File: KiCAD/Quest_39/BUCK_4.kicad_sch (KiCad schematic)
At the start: 32 parts, among them U16 AD626ANZ, U17 INA226, U18 LTM4611EV-PBF, U19 MCP4151-502E/SN

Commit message: Fixed INA226 schem. mistake and further layout work
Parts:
- added C63: 100nF, Capacitor_SMD:C_0603_1608Metric, symbol Device:C
- renumbered C56 to C59, C57 to C60, C58 to C61, C59 to C62, C60 to C64, C61 to C65, C62 to C66, C63 to C67, C64 to C68, C65 to C69, C66 to C70, C67 to C71, C68 to C72, C69 to C73
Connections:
- net +5V: now also C63.1
- net GND: now also C63.2
- net PV_POS: no longer C59.1, C60.1, C61.1, C62.1, R38.2, R40.1, R43.1, U18.A1 (VIN), U18.A2 (VIN), U18.A3 (VIN), U18.A4 (VIN), U18.A5 (VIN), U18.A6 (VIN), U18.B1 (VIN), U18.B2 (VIN), U18.B3 (VIN), U18.B4 (VIN), U18.B5 (VIN), U18.B6 (VIN), U18.C1 (VIN), U18.C2 (VIN), U18.C3 (VIN), U18.C4 (VIN), U18.C5 (VIN), U18.C6 (VIN)
- net Vin-: no longer TP28.1, U16.5 (OUT), U17.8 (Vbus)
- new net: TP28.1, U16.5 (OUT), U17.8 (Vbus)
- new net BUCK_VIN: C59.1, C60.1, C61.1, C62.1, R38.2, R40.1, R43.1, U18.A1 (VIN), U18.A2 (VIN), U18.A3 (VIN), U18.A4 (VIN), U18.A5 (VIN), U18.A6 (VIN), U18.B1 (VIN), U18.B2 (VIN), U18.B3 (VIN), U18.B4 (VIN), U18.B5 (VIN), U18.B6 (VIN), U18.C1 (VIN), U18.C2 (VIN), U18.C3 (VIN), U18.C4 (VIN), U18.C5 (VIN), U18.C6 (VIN)

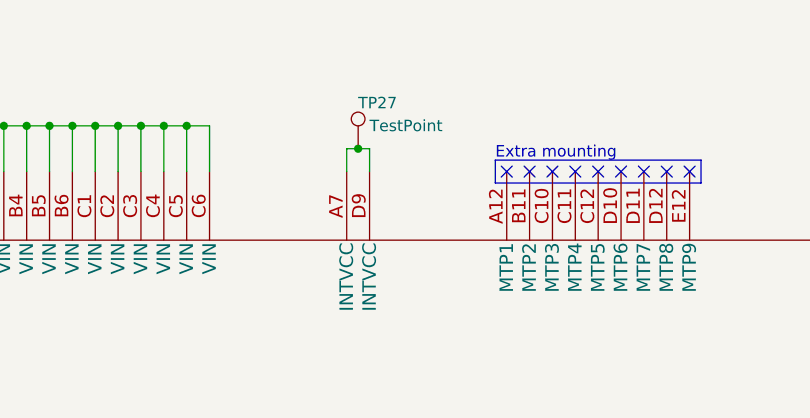
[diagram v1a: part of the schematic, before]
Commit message: Partial wiring of first buck converter section PCB layout
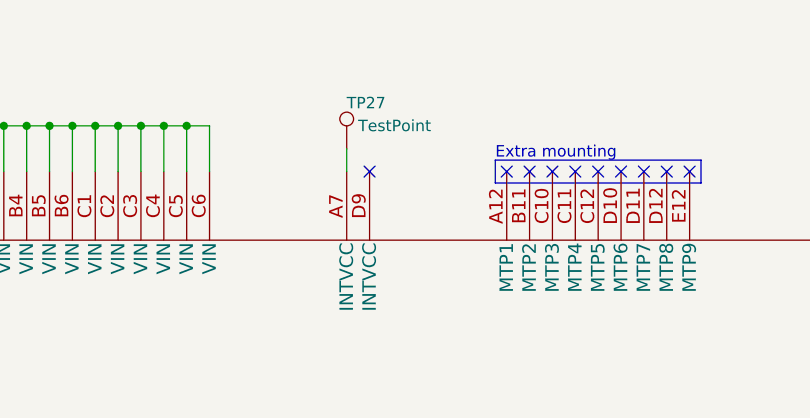
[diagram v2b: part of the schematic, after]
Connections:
- net at TP27.1, U18.A7 (INTVCC): no longer U18.D9 (INTVCC)
- no-connect marks 12 -> 13
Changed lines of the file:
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@@
   (junction (at 177.8 36.83) (diameter 0) (color 0 0 0 0)
-  )
-  (junction (at 234.95 39.37) (diameter 0) (color 0 0 0 0)
   )
   (junction (at 322.58 62.23) (diameter 0) (color 0 0 0 0)
@@
   (no_connect (at 104.14 88.9))
   (no_connect (at 266.7 41.91))
+  (no_connect (at 236.22 41.91))
   (no_connect (at 259.08 41.91))
   (no_connect (at 60.96 68.58))
@@
     (stroke (width 0) (type default) (color 0 0 0 0))
   )
+  (wire (pts (xy 233.68 41.91) (xy 233.68 39.37))
+    (stroke (width 0) (type default) (color 0 0 0 0))
+  )
   (wire (pts (xy 281.94 201.93) (xy 279.4 201.93))
     (stroke (width 0) (type default) (color 0 0 0 0))
@@
     (stroke (width 0) (type default) (color 0 0 0 0))
   )
-  (wire (pts (xy 233.68 41.91) (xy 233.68 39.37))
-    (stroke (width 0) (type default) (color 0 0 0 0))
-  )
   (wire (pts (xy 104.14 76.2) (xy 116.84 76.2))
     (stroke (width 0) (type default) (color 0 0 0 0))
@@
     (stroke (width 0) (type default) (color 0 0 0 0))
   )
-  (wire (pts (xy 236.22 39.37) (xy 236.22 41.91))
-    (stroke (width 0) (type default) (color 0 0 0 0))
-  )
   (wire (pts (xy 63.5 71.12) (xy 63.5 77.47))
     (stroke (width 0) (type default) (color 0 0 0 0))
@@
     (stroke (width 0) (type default) (color 0 0 0 0))
   )
-  (wire (pts (xy 233.68 39.37) (xy 234.95 39.37))
-    (stroke (width 0) (type default) (color 0 0 0 0))
-  )
   (wire (pts (xy 220.98 201.93) (xy 223.52 201.93))
     (stroke (width 0) (type default) (color 0 0 0 0))
@@
   )
   (wire (pts (xy 322.58 151.13) (xy 322.58 148.59))
-    (stroke (width 0) (type default) (color 0 0 0 0))
-  )
-  (wire (pts (xy 234.95 39.37) (xy 236.22 39.37))
     (stroke (width 0) (type default) (color 0 0 0 0))
   )
@@
   (hierarchical_label "CS" (shape input) (at 285.75 215.9 180)
     (effects (font (size 1.27 1.27)) (justify right))
+  )
+  (symbol (lib_id "Connector:TestPoint") (at 233.68 39.37 0) (unit 1)
+    (in_bom yes) (on_board yes)
+    (property "Reference" "TP27" (id 0) (at 233.68 34.29 0)
+      (effects (font (size 1.27 1.27)) (justify left))
+    )
+    (property "Value" "TestPoint" (id 1) (at 234.95 36.83 0)
+      (effects (font (size 1.27 1.27)) (justify left))
+    )
+    (property "Footprint" "TestPoint:TestPoint_Pad_D2.0mm" (id 2) (at 238.76 39.37 0)
+      (effects (font (size 1.27 1.27)) hide)
+    )
+    (property "Datasheet" "~" (id 3) (at 238.76 39.37 0)
+      (effects (font (size 1.27 1.27)) hide)
+    )
+    (pin "1")
   )
   (symbol (lib_id "Device:C") (at 396.24 165.1 0) (unit 1)
@@
       (effects (font (size 1.27 1.27)) hide)
     )
-    (pin "1")
-  )
-  (symbol (lib_id "Connector:TestPoint") (at 234.95 39.37 0) (unit 1)
-    (in_bom yes) (on_board yes)
-    (property "Reference" "TP27" (id 0) (at 234.95 34.29 0)
-      (effects (font (size 1.27 1.27)) (justify left))
-    )
-    (property "Value" "TestPoint" (id 1) (at 236.22 36.83 0)
-      (effects (font (size 1.27 1.27)) (justify left))
-    )
-    (property "Footprint" "TestPoint:TestPoint_Pad_D2.0mm" (id 2) (at 240.03 39.37 0)
-      (effects (font (size 1.27 1.27)) hide)
-    )
-    (property "Datasheet" "~" (id 3) (at 240.03 39.37 0)
-      (effects (font (size 1.27 1.27)) hide)
-    )

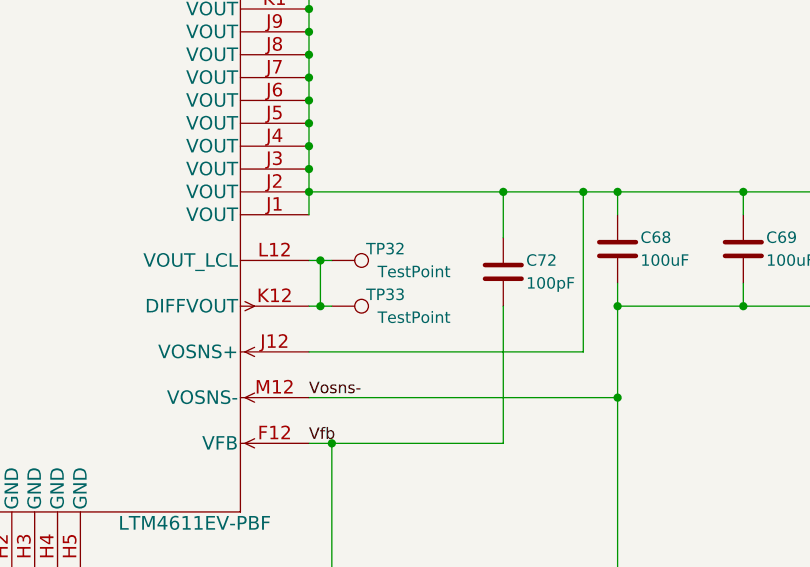
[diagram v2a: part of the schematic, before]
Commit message: Added 3rd buck converter section
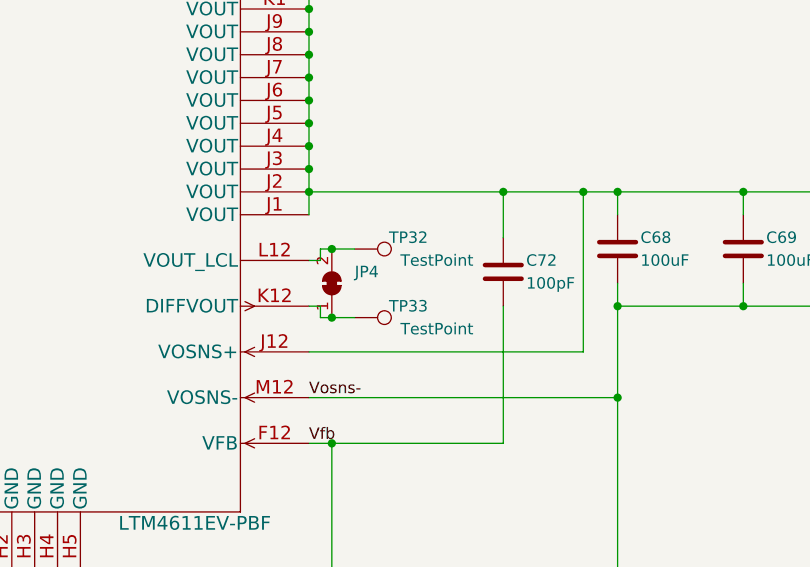
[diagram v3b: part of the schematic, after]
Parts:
- added JP4: SolderJumper_2_Bridged, Jumper:SolderJumper-2_P1.3mm_Bridged_RoundedPad1.0x1.5mm, symbol Jumper:SolderJumper_2_Bridged
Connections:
- net at TP32.1, U18.L12 (VOUT_LCL): now also JP4.2 (B); no longer TP33.1, U18.K12 (DIFFVOUT)
- new net: JP4.1 (A), TP33.1, U18.K12 (DIFFVOUT)
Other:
- moved on the sheet: TP32, TP33

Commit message: Placed 4th buck converter, started 5th.
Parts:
- U16: footprint Package_DIP:DIP-8_W8.89mm_SMDSocket_LongPads -> Package_DIP:DIP-8_W7.62mm_Socket_LongPads
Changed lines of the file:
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@@
       (effects (font (size 1.524 1.524)))
     )
-    (property "Footprint" "Package_DIP:DIP-8_W8.89mm_SMDSocket_LongPads" (id 2) (at 44.45 61.214 0)
+    (property "Footprint" "Package_DIP:DIP-8_W7.62mm_Socket_LongPads" (id 2) (at 44.45 61.214 0)
       (effects (font (size 1.524 1.524)) hide)
     )

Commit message: Added all the SolidWorks files, edited README
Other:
- title: (none) -> BUCK_4
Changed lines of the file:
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@@
 (kicad_sch (version 20211123) (generator eeschema)
   (paper "A3")
+  (title_block
+    (title "BUCK_4")
+    (date "2023-01-31")
+    (rev "1.0")
+  )
   (junction (at 322.58 82.55) (diameter 0) (color 0 0 0 0)
   )
